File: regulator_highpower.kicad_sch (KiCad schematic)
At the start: 13 parts, among them U12 I3A4W008A033V-001-R, U13 INA169

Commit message: finish layout
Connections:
- no-connect marks 1 -> 0
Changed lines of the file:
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@@
 		(color 0 0 0 0)
-	)
-	(no_connect
-		(at 58.42 53.34)
 	)
 	(wire

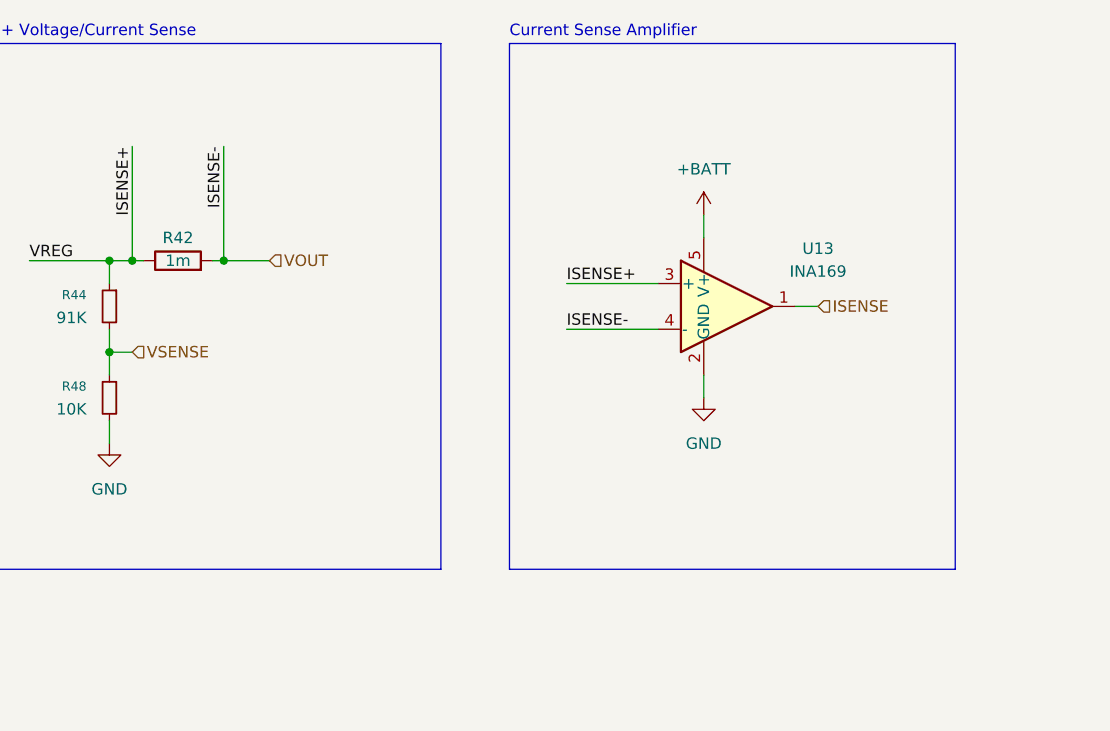
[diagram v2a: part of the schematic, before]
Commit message: optimize components, update schematic pdf
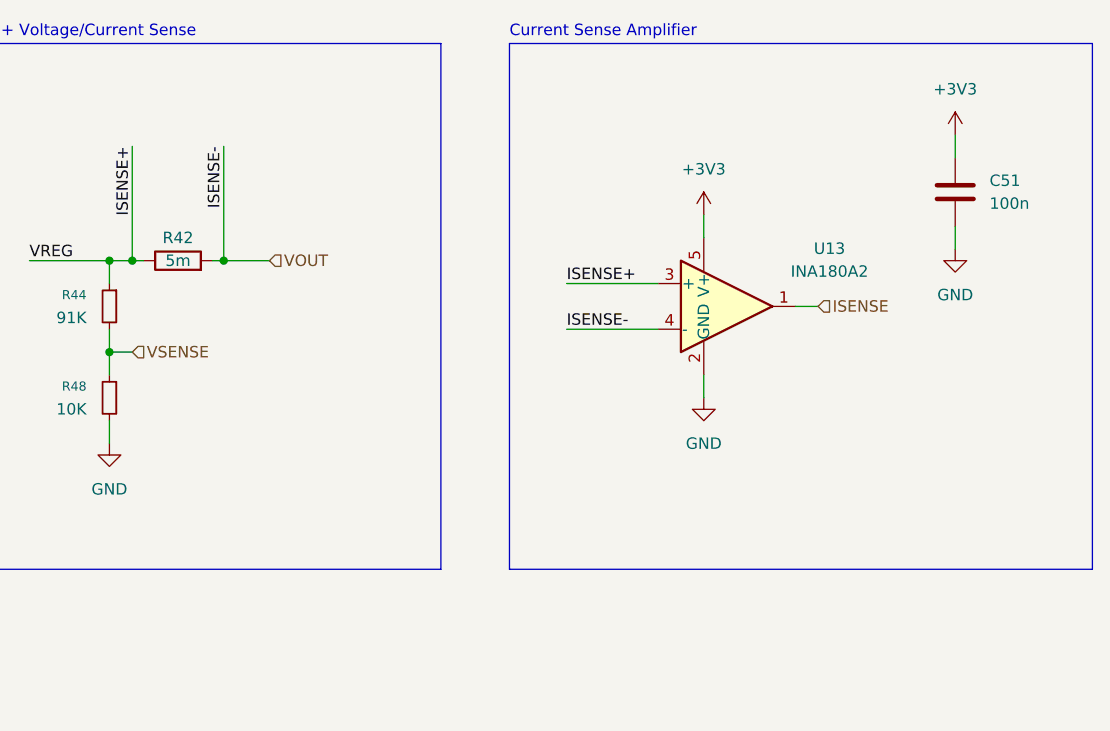
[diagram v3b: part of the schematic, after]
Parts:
- removed U13: INA169, Package_TO_SOT_SMD:SOT-23-5, symbol Amplifier_Current:INA169
- added C51: 100n, Capacitor_SMD:C_0402_1005Metric, symbol Device:C
- added U13: INA180A2, Package_TO_SOT_SMD:SOT-23-5, symbol Amplifier_Current:INA180A2
- R42: value 1m -> 5m
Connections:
- net +3V3: now also C51.1, U13.5 (V+)
- net GND: now also C51.2, U13.2 (GND)
- net ISENSE: now also U13.1
- net ISENSE+: now also U13.3 (+)
- net VOUT: now also U13.4 (-)
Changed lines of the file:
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@@
 	(rectangle
 		(start 200.66 21.59)
-		(end 250.19 80.01)
+		(end 265.43 80.01)
 		(stroke
 			(width 0)
@@
 	(wire
 		(pts
+			(xy 250.19 41.91) (xy 250.19 44.45)
+		)
+		(stroke
+			(width 0)
+			(type default)
+		)
+	)
+	(wire
+		(pts
 			(xy 81.28 45.72) (xy 81.28 43.18)
 		)
@@
 		(pts
 			(xy 105.41 54.61) (xy 105.41 55.88)
+		)
+		(stroke
+			(width 0)
+			(type default)
+		)
+	)
+	(wire
+		(pts
+			(xy 250.19 31.75) (xy 250.19 34.29)
 		)
 		(stroke
@@
 			)
 		)
-		(property "Value" "1m"
+		(property "Value" "5m"
 			(at 163.83 45.72 90)
 			(effects
@@
 	)
 	(symbol
-		(lib_id "Amplifier_Current:INA169")
+		(lib_id "power:+3V3")
+		(at 222.25 40.64 0)
+		(unit 1)
+		(exclude_from_sim no)
+		(in_bom yes)
+		(on_board yes)
+		(dnp no)
+		(fields_autoplaced yes)
+		(property "Reference" "#PWR072"
+			(at 222.25 44.45 0)
+			(effects
+				(font
+					(size 1.27 1.27)
+				)
+				(hide yes)
+			)
+		)
+		(property "Value" "+3V3"
+			(at 222.25 35.56 0)
+			(effects
+				(font
+					(size 1.27 1.27)
+				)
+			)
+		)
+		(property "Footprint" ""
+			(at 222.25 40.64 0)
+			(effects
+				(font
+					(size 1.27 1.27)
+				)
+				(hide yes)
+			)
+		)
+		(property "Datasheet" ""
+			(at 222.25 40.64 0)
+			(effects
+				(font
+					(size 1.27 1.27)
+				)
+				(hide yes)
+			)
+		)
+		(property "Description" "Power symbol creates a global label with name \"+3V3\""
+			(at 222.25 40.64 0)
+			(effects
+				(font
+					(size 1.27 1.27)
+				)
+				(hide yes)
+			)
+		)
+		(pin "1"
+		)
+		(instances
+			(project "vrb"
+				(path "/59a9b615-ea12-4a8c-9228-b32f861e8d75/eb1e4a76-3344-4a3b-8543-2ea356ffbe51"
+					(reference "#PWR072")
+					(unit 1)
+				)
+			)
+		)
+	)
+	(symbol
+		(lib_id "Amplifier_Current:INA180A2")
 		(at 224.79 50.8 0)
 		(unit 1)
@@
 		(fields_autoplaced yes)
 		(property "Reference" "U13"
-			(at 234.95 44.3798 0)
-			(effects
-				(font
-					(size 1.27 1.27)
-				)
-			)
-		)
-		(property "Value" "INA169"
-			(at 234.95 46.9198 0)
+			(at 236.22 44.3798 0)
+			(effects
+				(font
+					(size 1.27 1.27)
+				)
+			)
+		)
+		(property "Value" "INA180A2"
+			(at 236.22 46.9198 0)
 			(effects
 				(font
@@
 		)
 		(property "Footprint" "Package_TO_SOT_SMD:SOT-23-5"
+			(at 226.06 49.53 0)
+			(effects
+				(font
+					(size 1.27 1.27)
+				)
+				(hide yes)
+			)
+		)
+		(property "Datasheet" "http://www.ti.com/lit/ds/symlink/ina180.pdf"
+			(at 228.6 46.99 0)
+			(effects
+				(font
+					(size 1.27 1.27)
+				)
+				(hide yes)
+			)
+		)
+		(property "Description" "Current Sense Amplifier, 1 Circuit, Rail-to-Rail, 26V, Gain 50 V/V, SOT-23-5"
 			(at 224.79 50.8 0)
 			(effects
@@
 			)
 		)
-		(property "Datasheet" "http://www.ti.com/lit/ds/symlink/ina169.pdf"
-			(at 224.79 50.673 0)
-			(effects
-				(font
-					(size 1.27 1.27)
-				)
-				(hide yes)
-			)
-		)
-		(property "Description" "High-Side Measurement Current Shunt Monitor, 60V, SOT-23-5"
-			(at 224.79 50.8 0)
-			(effects
-				(font
-					(size 1.27 1.27)
-				)
-				(hide yes)
-			)
+		(pin "3"
+		)
+		(pin "2"
+		)
+		(pin "1"
 		)
 		(pin "5"
@@
 		(pin "4"
 		)
-		(pin "3"
-		)
-		(pin "2"
-		)
-		(pin "1"
-		)
-		(instances
-			(project "vrb"
+		(instances
+			(project ""
 				(path "/59a9b615-ea12-4a8c-9228-b32f861e8d75/eb1e4a76-3344-4a3b-8543-2ea356ffbe51"
 					(reference "U13")
@@
 				(path "/59a9b615-ea12-4a8c-9228-b32f861e8d75/eb1e4a76-3344-4a3b-8543-2ea356ffbe51"
 					(reference "D11")
+					(unit 1)
+				)
+			)
+		)
+	)
+	(symbol
+		(lib_id "power:GND")
+		(at 250.19 44.45 0)
+		(unit 1)
+		(exclude_from_sim no)
+		(in_bom yes)
+		(on_board yes)
+		(dnp no)
+		(fields_autoplaced yes)
+		(property "Reference" "#PWR0177"
+			(at 250.19 50.8 0)
+			(effects
+				(font
+					(size 1.27 1.27)
+				)
+				(hide yes)
+			)
+		)
+		(property "Value" "GND"
+			(at 250.19 49.53 0)
+			(effects
+				(font
+					(size 1.27 1.27)
+				)
+			)
+		)
+		(property "Footprint" ""
+			(at 250.19 44.45 0)
+			(effects
+				(font
+					(size 1.27 1.27)
+				)
+				(hide yes)
+			)
+		)
+		(property "Datasheet" ""
+			(at 250.19 44.45 0)
+			(effects
+				(font
+					(size 1.27 1.27)
+				)
+				(hide yes)
+			)
+		)
+		(property "Description" "Power symbol creates a global label with name \"GND\" , ground"
+			(at 250.19 44.45 0)
+			(effects
+				(font
+					(size 1.27 1.27)
+				)
+				(hide yes)
+			)
+		)
+		(pin "1"
+		)
+		(instances
+			(project "vrb"
+				(path "/59a9b615-ea12-4a8c-9228-b32f861e8d75/eb1e4a76-3344-4a3b-8543-2ea356ffbe51"
+					(reference "#PWR0177")
+					(unit 1)
+				)
+			)
+		)
+	)
+	(symbol
+		(lib_id "Device:C")
+		(at 250.19 38.1 0)
+		(unit 1)
+		(exclude_from_sim no)
+		(in_bom yes)
+		(on_board yes)
+		(dnp no)
+		(fields_autoplaced yes)
+		(property "Reference" "C51"
+			(at 254 36.8299 0)
+			(effects
+				(font
+					(size 1.27 1.27)
+				)
+				(justify left)
+			)
+		)
+		(property "Value" "100n"
+			(at 254 39.3699 0)
+			(effects
+				(font
+					(size 1.27 1.27)
+				)
+				(justify left)
+			)
+		)
+		(property "Footprint" "Capacitor_SMD:C_0402_1005Metric"
+			(at 251.1552 41.91 0)
+			(effects
+				(font
+					(size 1.27 1.27)
+				)
+				(hide yes)
+			)
+		)
+		(property "Datasheet" "~"
+			(at 250.19 38.1 0)
+			(effects
+				(font
+					(size 1.27 1.27)
+				)
+				(hide yes)
+			)
+		)
+		(property "Description" "Unpolarized capacitor"
+			(at 250.19 38.1 0)
+			(effects
+				(font
+					(size 1.27 1.27)
+				)
+				(hide yes)
+			)
+		)
+		(pin "1"
+		)
+		(pin "2"
+		)
+		(instances
+			(project "vrb"
+				(path "/59a9b615-ea12-4a8c-9228-b32f861e8d75/eb1e4a76-3344-4a3b-8543-2ea356ffbe51"
+					(reference "C51")
 					(unit 1)
 				)
@@
 	)
 	(symbol
-		(lib_id "power:+BATT")
-		(at 222.25 40.64 0)
-		(unit 1)
-		(exclude_from_sim no)
-		(in_bom yes)
-		(on_board yes)
-		(dnp no)
-		(fields_autoplaced yes)
-		(property "Reference" "#PWR072"
-			(at 222.25 44.45 0)
-			(effects
-				(font
-					(size 1.27 1.27)
-				)
-				(hide yes)
-			)
-		)
-		(property "Value" "+BATT"
-			(at 222.25 35.56 0)
-			(effects
-				(font
-					(size 1.27 1.27)
-				)
-			)
-		)
-		(property "Footprint" ""
-			(at 222.25 40.64 0)
-			(effects
-				(font
-					(size 1.27 1.27)
-				)
-				(hide yes)
-			)
-		)
-		(property "Datasheet" ""
-			(at 222.25 40.64 0)
-			(effects
-				(font
-					(size 1.27 1.27)
-				)
-				(hide yes)
-			)
-		)
-		(property "Description" "Power symbol creates a global label with name \"+BATT\""
-			(at 222.25 40.64 0)
-			(effects
-				(font
-					(size 1.27 1.27)
-				)
-				(hide yes)
-			)
-		)
-		(pin "1"
-		)
-		(instances
-			(project "vrb"
-				(path "/59a9b615-ea12-4a8c-9228-b32f861e8d75/eb1e4a76-3344-4a3b-8543-2ea356ffbe51"
-					(reference "#PWR072")
-					(unit 1)
-				)
-			)
-		)
-	)
-	(symbol
 		(lib_id "Device:C_Polarized")
 		(at 105.41 49.53 0)
@@
 					(unit 1)
 				)
+			)
+		)
+	)
+	(symbol
+		(lib_id "power:+3V3")
+		(at 250.19 31.75 0)
+		(unit 1)
+		(exclude_from_sim no)
+		(in_bom yes)
+		(on_board yes)
+		(dnp no)
+		(fields_autoplaced yes)
+		(property "Reference" "#PWR0176"
+			(at 250.19 35.56 0)
+			(effects
+				(font
+					(size 1.27 1.27)
+				)
+				(hide yes)
+			)
+		)
+		(property "Value" "+3V3"
+			(at 250.19 26.67 0)
+			(effects
+				(font
+					(size 1.27 1.27)
+				)
+			)
+		)
+		(property "Footprint" ""
+			(at 250.19 31.75 0)
+			(effects
+				(font
+					(size 1.27 1.27)
+				)
+				(hide yes)
+			)
+		)
+		(property "Datasheet" ""
+			(at 250.19 31.75 0)
+			(effects
+				(font
+					(size 1.27 1.27)
+				)
+				(hide yes)
+			)
+		)
+		(property "Description" "Power symbol creates a global label with name \"+3V3\""
+			(at 250.19 31.75 0)
+			(effects
+				(font
+					(size 1.27 1.27)
+				)
+				(hide yes)
+			)
+		)
+		(pin "1"
+		)
+		(instances
+			(project "vrb"
+				(path "/59a9b615-ea12-4a8c-9228-b32f861e8d75/eb1e4a76-3344-4a3b-8543-2ea356ffbe51"
+					(reference "#PWR0176")
+					(unit 1)
+				)
